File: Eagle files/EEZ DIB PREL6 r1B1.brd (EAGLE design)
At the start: 146 x 95 mm, 66 parts, among them IC1 STM32F030C6T6, IC2 74HC1G126DBVT, IC3 M24C32-WMN6P, IC4 LP2985-33DBVR, K1 RT424005, K2 RT424005, K3 RT424005, K4 RT424005, K5 RT424005, K6 RT424005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

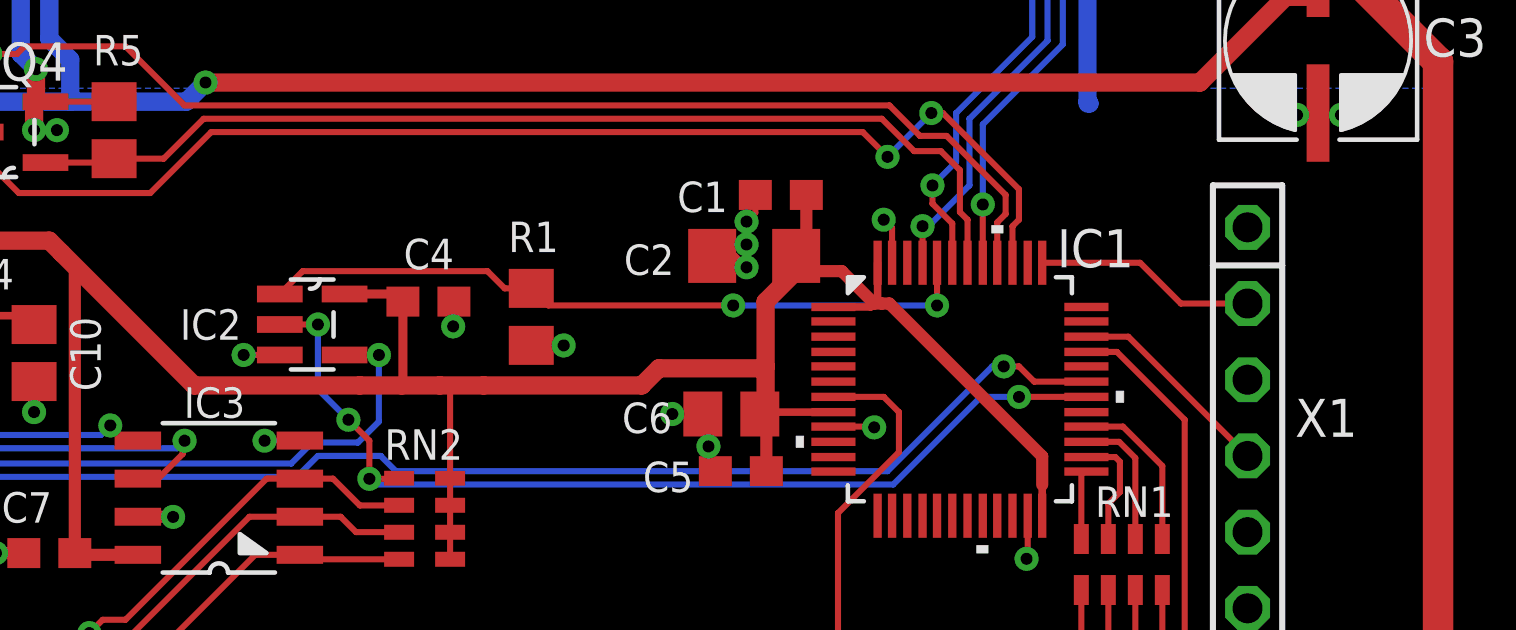
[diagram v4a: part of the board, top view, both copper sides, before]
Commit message: IC2 package update
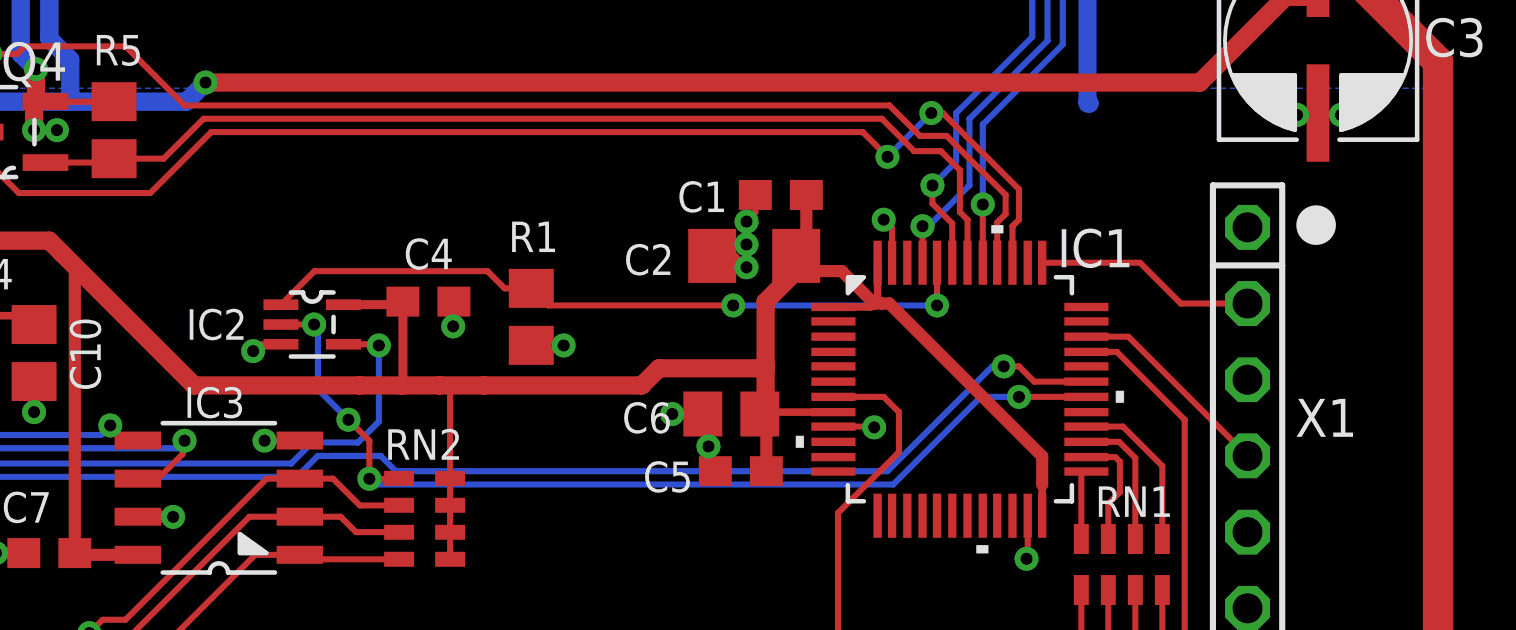
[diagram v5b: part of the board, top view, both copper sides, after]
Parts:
- IC2: value 74HC1G126DBVT -> 74HC1G126GW,125; device EEZ_TI:SOT23-5 -> EEZ_Lib1:SOT65P210X110-5N
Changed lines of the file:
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@@
 <setting verticaltext="up"/>
 </settings>
-<grid distance="0.1" unitdist="mm" unit="mm" style="lines" multiple="40" display="no" altdistance="2.5" altunitdist="mil" altunit="mil"/>
+<grid distance="2.5" unitdist="mil" unit="mil" style="lines" multiple="40" display="no" altdistance="2.5" altunitdist="mil" altunit="mil"/>
 <layers>
 <layer number="1" name="Top" color="3" fill="1" visible="yes" active="yes"/>
@@
 <layer number="49" name="Reference" color="7" fill="1" visible="no" active="yes"/>
 <layer number="50" name="dxf" color="7" fill="1" visible="no" active="no"/>
-<layer number="51" name="tDocu" color="14" fill="1" visible="yes" active="yes"/>
+<layer number="51" name="tDocu" color="14" fill="1" visible="no" active="yes"/>
 <layer number="52" name="bDocu" color="5" fill="1" visible="no" active="yes"/>
 <layer number="53" name="tGND_GNDA" color="7" fill="9" visible="no" active="no"/>
@@
 <wire x1="4.064" y1="72.263" x2="4.064" y2="73.025" width="0.1" layer="20"/>
 <wire x1="24.892" y1="72.263" x2="24.892" y2="73.025" width="0.1" layer="20"/>
+<circle x="135" y="21.6" radius="0.3302" width="0.6604" layer="21"/>
 </plain>
 <attributes>
@@
 <attribute name="VALUE" x="103.9495" y="18.542" size="1.016" layer="27" ratio="10"/>
 </element>
-<element name="IC2" library="EEZ_TI" package="SOT23-5" value="74HC1G126DBVT" x="101.5365" y="18.288" smashed="yes">
-<attribute name="NAME" x="97.1296" y="17.78" size="1.016" layer="25" ratio="10" rot="SR0"/>
+<element name="IC2" library="EEZ_Lib1" package="SOT65P210X110-5N" value="74HC1G126GW,125" x="101.5365" y="18.288" smashed="yes">
+<attribute name="NAME" x="97.3296" y="17.78" size="1.016" layer="25" ratio="10" rot="SR0"/>
 <attribute name="VALUE" x="96.3676" y="17.907" size="0.6096" layer="27" ratio="10" rot="SR0"/>
 </element>
@@
 <via x="106.2355" y="18.2245" extent="1-16" drill="0.4" shape="square"/>
 <wire x1="106.26" y1="19.05" x2="106.2355" y2="18.2245" width="0.2032" layer="1"/>
-<via x="99.2505" y="17.272" extent="1-16" drill="0.4" shape="square"/>
-<wire x1="100.457" y1="17.272" x2="99.2505" y2="17.272" width="0.2032" layer="1"/>
+<via x="99.568" y="17.399" extent="1-16" drill="0.4" shape="square"/>
 <wire x1="91.9235" y1="10.668" x2="90.9955" y2="10.668" width="0.4064" layer="1"/>
 <via x="96.901" y="11.8745" extent="1-16" drill="0.4" shape="square"/>
@@
 <via x="86.6775" y="20.701" extent="1-16" drill="0.4" shape="square"/>
 <contactref element="X1" pad="3"/>
+<wire x1="100.4951" y1="17.6276" x2="99.7966" y2="17.6276" width="0.2032" layer="1"/>
+<wire x1="99.7966" y1="17.6276" x2="99.568" y2="17.399" width="0.2032" layer="1"/>
 </signal>
 <signal name="DIB_A0">
@@
 <wire x1="95.725" y1="10.6095" x2="93.682" y2="10.6095" width="0.4064" layer="1"/>
 <wire x1="93.682" y1="10.6095" x2="93.6235" y2="10.668" width="0.4064" layer="1"/>
-<wire x1="102.616" y1="19.304" x2="104.306" y2="19.304" width="0.3048" layer="1"/>
-<wire x1="104.306" y1="19.304" x2="104.56" y2="19.05" width="0.3048" layer="1"/>
 <wire x1="118.9101" y1="15.367" x2="117.028" y2="15.367" width="0.254" layer="1"/>
 <wire x1="117.028" y1="15.367" x2="116.6495" y2="14.9885" width="0.254" layer="1"/>
@@
 <wire x1="93.6235" y1="10.668" x2="93.6235" y2="20.232" width="0.4064" layer="1"/>
 <wire x1="93.6235" y1="20.232" x2="93.18625" y2="20.66925" width="0.4064" layer="1"/>
+<wire x1="102.5779" y1="18.9484" x2="104.4584" y2="18.9484" width="0.3048" layer="1"/>
+<wire x1="104.4584" y1="18.9484" x2="104.56" y2="19.05" width="0.3048" layer="1"/>
 </signal>
 <signal name="N$70">
@@
 <wire x1="108.839" y1="19.492" x2="107.9525" y2="19.492" width="0.2032" layer="1"/>
 <wire x1="107.9525" y1="19.492" x2="107.3785" y2="20.066" width="0.2032" layer="1"/>
-<wire x1="107.3785" y1="20.066" x2="101.219" y2="20.066" width="0.2032" layer="1"/>
-<wire x1="101.219" y1="20.066" x2="100.457" y2="19.304" width="0.2032" layer="1"/>
 <wire x1="115.57" y1="18.923" x2="109.408" y2="18.923" width="0.2032" layer="1"/>
 <wire x1="109.408" y1="18.923" x2="108.839" y2="19.492" width="0.2032" layer="1"/>
+<wire x1="107.3785" y1="20.066" x2="101.6127" y2="20.066" width="0.2032" layer="1"/>
+<wire x1="101.6127" y1="20.066" x2="100.4951" y2="18.9484" width="0.2032" layer="1"/>
 </signal>
 <signal name="DIB_CSA">
@@
 <wire x1="104.433" y1="13.161" x2="104.22" y2="13.161" width="0.2032" layer="1"/>
 <via x="102.743" y="15.113" extent="1-16" drill="0.4" shape="octagon"/>
-<via x="101.727" y="18.288" extent="1-16" drill="0.4" shape="octagon"/>
-<wire x1="101.727" y1="18.288" x2="100.457" y2="18.288" width="0.2032" layer="1"/>
+<via x="101.6" y="18.288" extent="1-16" drill="0.4" shape="octagon"/>
+<wire x1="101.6" y1="18.288" x2="100.4951" y2="18.288" width="0.2032" layer="1"/>
 <via x="103.4415" y="13.1445" extent="1-16" drill="0.4" shape="octagon"/>
 <wire x1="104.22" y1="13.161" x2="104.2035" y2="13.1445" width="0.2032" layer="1"/>
 <wire x1="104.2035" y1="13.1445" x2="103.4415" y2="13.1445" width="0.2032" layer="1"/>
-<wire x1="101.727" y1="18.288" x2="101.727" y2="16.129" width="0.2032" layer="16"/>
 <wire x1="101.727" y1="16.129" x2="102.743" y2="15.113" width="0.2032" layer="16"/>
 <wire x1="103.4415" y1="13.1445" x2="103.4415" y2="14.4145" width="0.2032" layer="1"/>
@@
 <wire x1="103.632" y1="12.954" x2="103.4415" y2="13.1445" width="0.2032" layer="16"/>
 <wire x1="125.095" y1="15.875" x2="123.825" y2="15.875" width="0.2032" layer="16"/>
+<wire x1="101.727" y1="16.129" x2="101.727" y2="18.161" width="0.2032" layer="16"/>
+<wire x1="101.727" y1="18.161" x2="101.6" y2="18.288" width="0.2032" layer="16"/>
 </signal>
 <signal name="SWDIO">
@@
 <wire x1="87.54" y1="12.5" x2="88.8905" y2="12.5" width="0.2032" layer="16"/>
 <wire x1="88.8905" y1="12.5" x2="90.043" y2="13.6525" width="0.2032" layer="16"/>
-<via x="103.759" y="17.272" extent="1-16" drill="0.4" shape="octagon"/>
-<wire x1="103.759" y1="17.272" x2="102.616" y2="17.272" width="0.2032" layer="1"/>
+<via x="103.759" y="17.5895" extent="1-16" drill="0.4" shape="octagon"/>
 <wire x1="100.838" y1="13.6525" x2="90.043" y2="13.6525" width="0.2032" layer="16"/>
 <wire x1="103.759" y1="15.0495" x2="103.0605" y2="14.351" width="0.2032" layer="16"/>
 <wire x1="103.0605" y1="14.351" x2="101.5365" y2="14.351" width="0.2032" layer="16"/>
 <wire x1="101.5365" y1="14.351" x2="100.838" y2="13.6525" width="0.2032" layer="16"/>
-<wire x1="103.759" y1="17.272" x2="103.759" y2="15.0495" width="0.2032" layer="16"/>
+<wire x1="103.759" y1="17.5895" x2="103.759" y2="15.0495" width="0.2032" layer="16"/>
+<wire x1="102.5779" y1="17.6276" x2="103.7209" y2="17.6276" width="0.2032" layer="1"/>
+<wire x1="103.7209" y1="17.6276" x2="103.759" y2="17.5895" width="0.2032" layer="1"/>
 </signal>
 <signal name="N$1">
